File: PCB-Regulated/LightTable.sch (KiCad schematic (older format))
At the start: 22 parts, among them CON1 BARREL_JACK, P1 CONN_2_V, P2 CONN_01X01, P3 CONN_01X01, P4 CONN_01X01, P5 CONN_01X01, P6 CONN_01X01, P7 CONN_01X01, P8 CONN_4_V, U1 MosfetIRF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

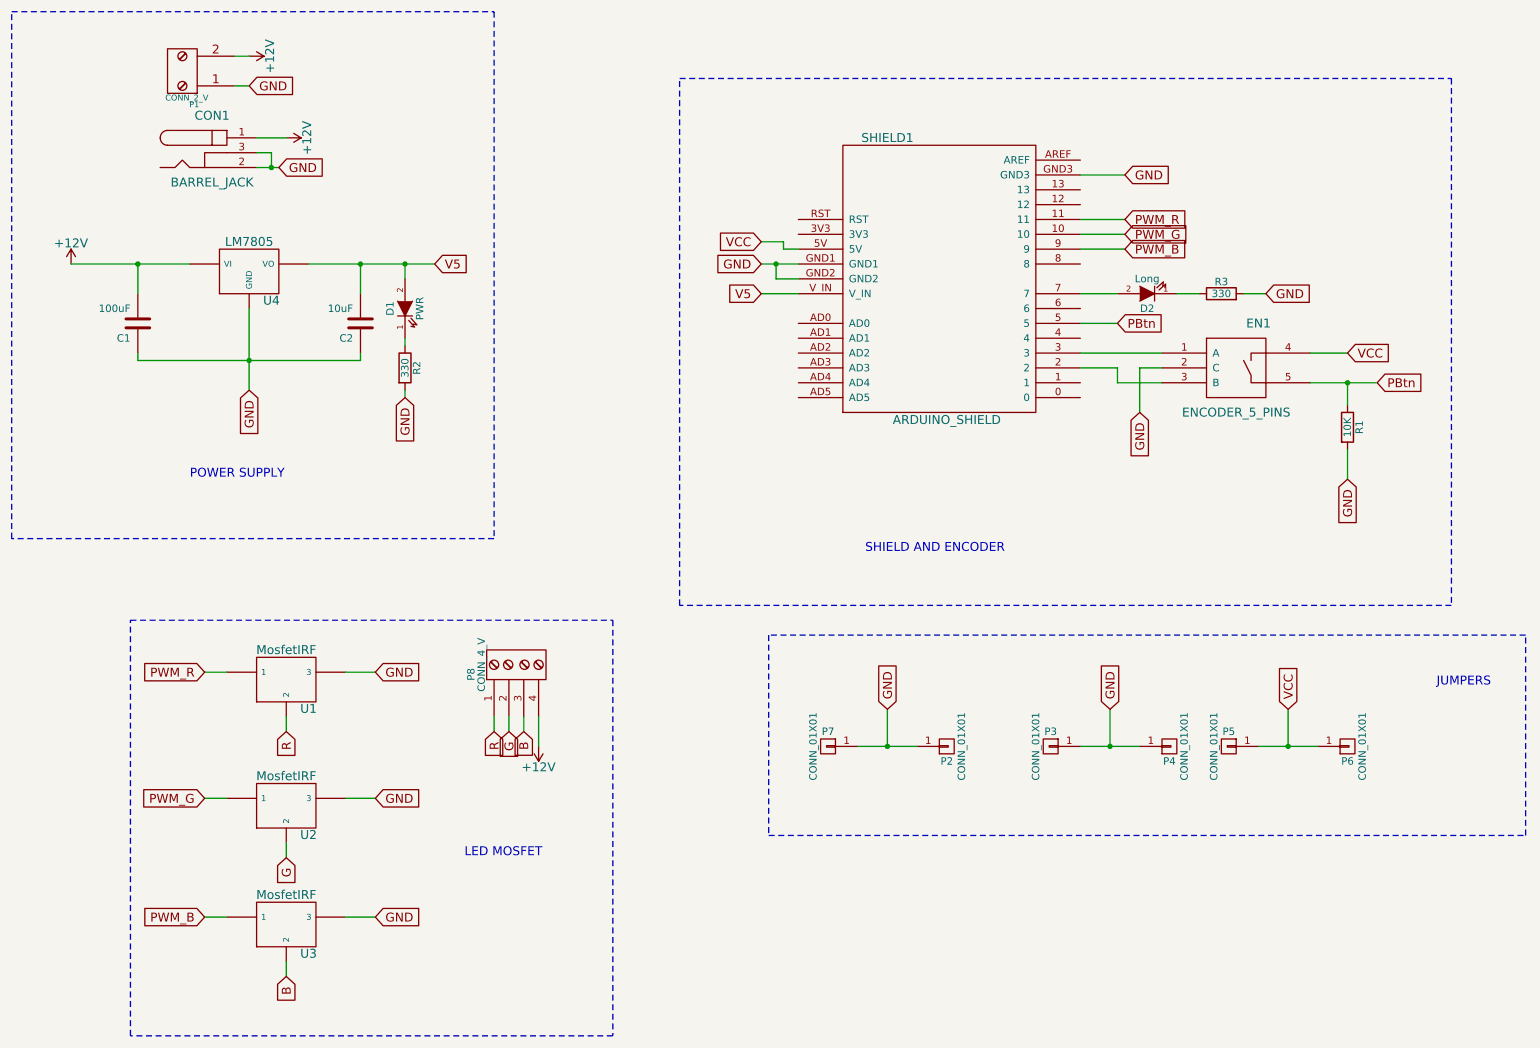
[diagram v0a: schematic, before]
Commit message: Fixed wrong placement of shield
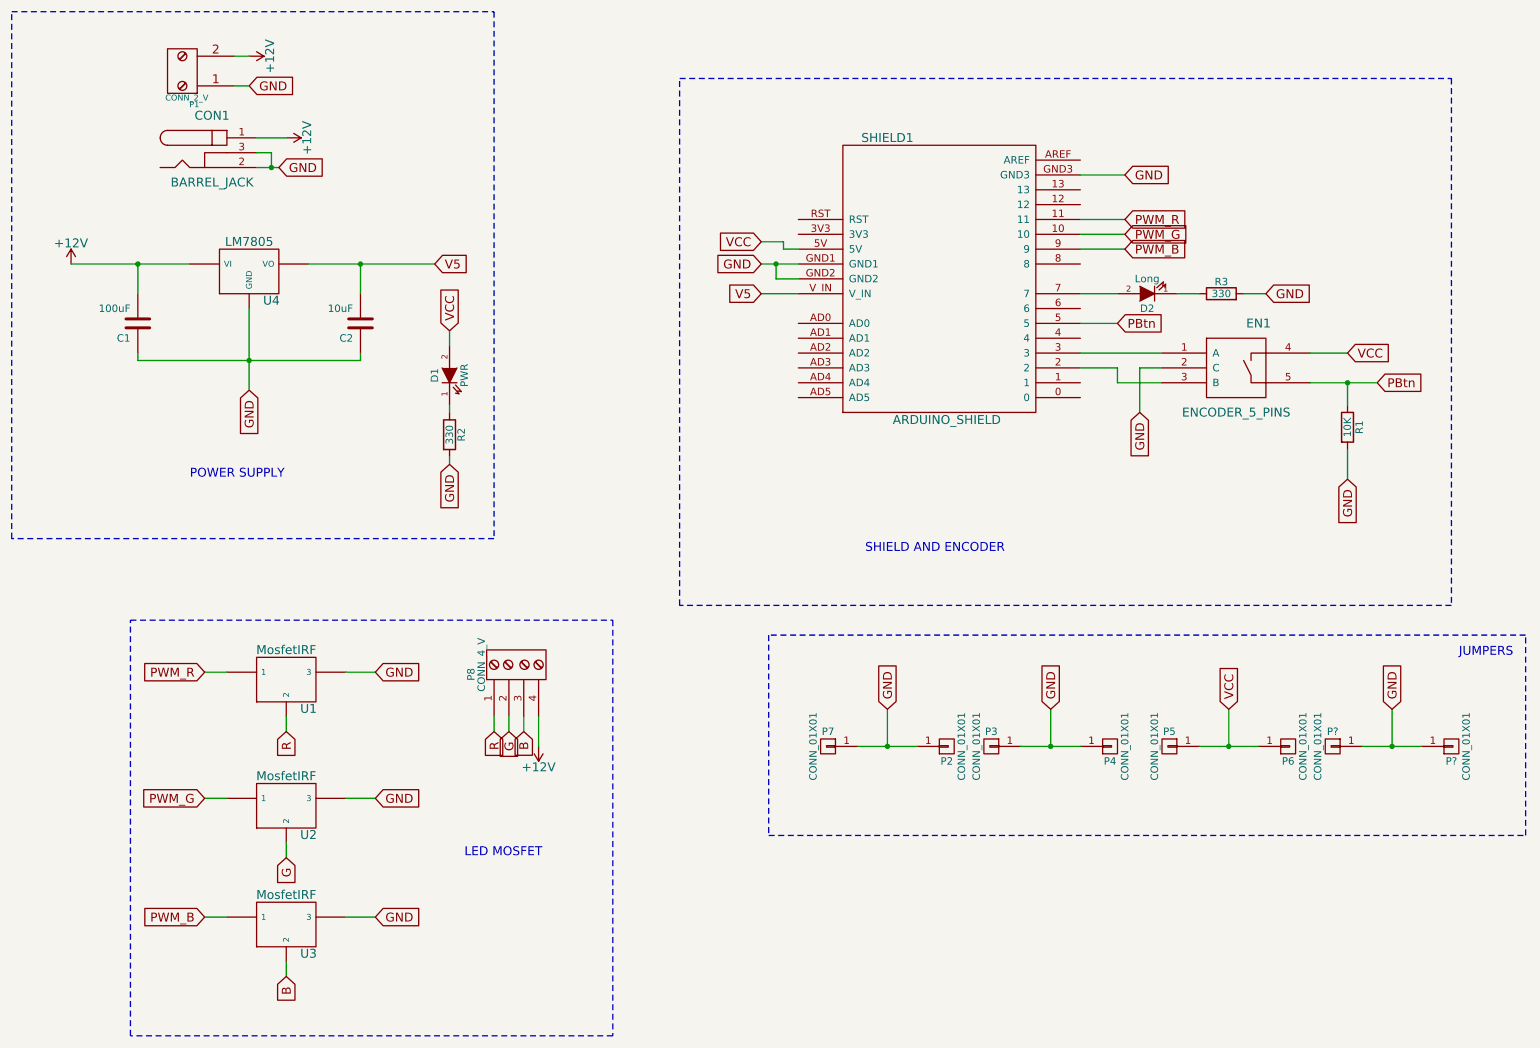
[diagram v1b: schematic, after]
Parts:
- added P? (x2): CONN_01X01, library:header1x01, symbol CONN_01X01
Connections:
- net GND: now also P?.1 (P1), P?.1 (P1)
- net V5: no longer D1.2 (A)
- net VCC: now also D1.2 (A)
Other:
- moved on the sheet: D1, P3, P4, P5, P6, R2
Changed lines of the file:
@@
 L CONN_01X01 P4
 U 1 1 55CC9A8E
-P 8350 5550
-F 0 "P4" H 8350 5650 50  0000 C CNN
-F 1 "CONN_01X01" V 8450 5550 50  0000 C CNN
-F 2 "library:header1x01" H 8350 5550 60  0001 C CNN
-F 3 "" H 8350 5550 60  0000 C CNN
-	1    8350 5550
+P 7950 5550
+F 0 "P4" H 7950 5650 50  0000 C CNN
+F 1 "CONN_01X01" V 8050 5550 50  0000 C CNN
+F 2 "library:header1x01" H 7950 5550 60  0001 C CNN
+F 3 "" H 7950 5550 60  0000 C CNN
+	1    7950 5550
 	1    0    0    1
 $EndComp
@@
 L CONN_01X01 P3
 U 1 1 55CC9A94
-P 7550 5550
-F 0 "P3" H 7550 5650 50  0000 C CNN
-F 1 "CONN_01X01" V 7650 5550 50  0000 C CNN
-F 2 "library:header1x01" H 7550 5550 60  0001 C CNN
-F 3 "" H 7550 5550 60  0000 C CNN
-	1    7550 5550
+P 7150 5550
+F 0 "P3" H 7150 5650 50  0000 C CNN
+F 1 "CONN_01X01" V 7250 5550 50  0000 C CNN
+F 2 "library:header1x01" H 7150 5550 60  0001 C CNN
+F 3 "" H 7150 5550 60  0000 C CNN
+	1    7150 5550
 	-1   0    0    -1
 $EndComp
 Wire Wire Line
-	7750 5550 8150 5550
+	7350 5550 7750 5550
 Wire Wire Line
-	7950 5550 7950 5300
-Connection ~ 7950 5550
-Text GLabel 7950 5300 1    60   Input ~ 0
+	7550 5550 7550 5300
+Connection ~ 7550 5550
+Text GLabel 7550 5300 1    60   Input ~ 0
 GND
 $Comp
 L CONN_01X01 P6
 U 1 1 55CC9B1E
-P 9550 5550
-F 0 "P6" H 9550 5650 50  0000 C CNN
-F 1 "CONN_01X01" V 9650 5550 50  0000 C CNN
-F 2 "library:header1x01" H 9550 5550 60  0001 C CNN
-F 3 "" H 9550 5550 60  0000 C CNN
-	1    9550 5550
+P 9150 5550
+F 0 "P6" H 9150 5650 50  0000 C CNN
+F 1 "CONN_01X01" V 9250 5550 50  0000 C CNN
+F 2 "library:header1x01" H 9150 5550 60  0001 C CNN
+F 3 "" H 9150 5550 60  0000 C CNN
+	1    9150 5550
 	1    0    0    1
 $EndComp
@@
 L CONN_01X01 P5
 U 1 1 55CC9B24
-P 8750 5550
-F 0 "P5" H 8750 5650 50  0000 C CNN
-F 1 "CONN_01X01" V 8850 5550 50  0000 C CNN
-F 2 "library:header1x01" H 8750 5550 60  0001 C CNN
-F 3 "" H 8750 5550 60  0000 C CNN
-	1    8750 5550
+P 8350 5550
+F 0 "P5" H 8350 5650 50  0000 C CNN
+F 1 "CONN_01X01" V 8450 5550 50  0000 C CNN
+F 2 "library:header1x01" H 8350 5550 60  0001 C CNN
+F 3 "" H 8350 5550 60  0000 C CNN
+	1    8350 5550
 	-1   0    0    -1
 $EndComp
 Wire Wire Line
-	8950 5550 9350 5550
+	8550 5550 8950 5550
 Wire Wire Line
-	9150 5550 9150 5300
-Connection ~ 9150 5550
-Text GLabel 9150 5300 1    60   Input ~ 0
+	8750 5550 8750 5300
+Connection ~ 8750 5550
+Text GLabel 8750 5300 1    60   Input ~ 0
 VCC
 Wire Notes Line
@@
 Wire Notes Line
 	10750 4800 5650 4800
-Text Notes 10150 5150 0    60   ~ 0
+Text Notes 10300 4950 0    60   ~ 0
 JUMPERS
 $Comp
@@
 L LED D1
 U 1 1 55CC841D
-P 3200 2600
-F 0 "D1" H 3200 2700 50  0000 C CNN
-F 1 "PWR" H 3200 2500 50  0000 C CNN
-F 2 "LEDs:LED-5MM" H 3200 2600 60  0001 C CNN
-F 3 "" H 3200 2600 60  0000 C CNN
-	1    3200 2600
+P 3500 3050
+F 0 "D1" H 3500 3150 50  0000 C CNN
+F 1 "PWR" H 3500 2950 50  0000 C CNN
+F 2 "LEDs:LED-5MM" H 3500 3050 60  0001 C CNN
+F 3 "" H 3500 3050 60  0000 C CNN
+	1    3500 3050
 	0    -1   -1   0
 $EndComp
-Connection ~ 3200 2300
 $Comp
 L R R2
 U 1 1 55CC852C
-P 3200 3000
-F 0 "R2" V 3280 3000 50  0000 C CNN
-F 1 "330" V 3200 3000 50  0000 C CNN
-F 2 "Resistors_ThroughHole:Resistor_Horizontal_RM10mm" V 3130 3000 30  0001 C CNN
-F 3 "" H 3200 3000 30  0000 C CNN
-	1    3200 3000
+P 3500 3450
+F 0 "R2" V 3580 3450 50  0000 C CNN
+F 1 "330" V 3500 3450 50  0000 C CNN
+F 2 "Resistors_ThroughHole:Resistor_Horizontal_RM10mm" V 3430 3450 30  0001 C CNN
+F 3 "" H 3500 3450 30  0000 C CNN
+	1    3500 3450
 	1    0    0    -1
 $EndComp
-Text GLabel 3200 3200 3    60   Input ~ 0
+Text GLabel 3500 3650 3    60   Input ~ 0
 GND
 Wire Wire Line
-	3200 3200 3200 3150
+	3500 3650 3500 3600
 Wire Wire Line
-	3200 2850 3200 2800
-Wire Wire Line
-	3200 2400 3200 2300
+	3500 3300 3500 3250
 Text GLabel 8000 2700 2    60   Input ~ 0
 PBtn
@@
 Wire Wire Line
 	8850 2500 9000 2500
+Text GLabel 3500 2750 1    60   Input ~ 0
+VCC
+Wire Wire Line
+	3500 2750 3500 2850
+$Comp
+L CONN_01X01 P?
+U 1 1 55D5B06A
+P 10250 5550
+F 0 "P?" H 10250 5650 50  0000 C CNN
+F 1 "CONN_01X01" V 10350 5550 50  0000 C CNN
+F 2 "library:header1x01" H 10250 5550 60  0001 C CNN
+F 3 "" H 10250 5550 60  0000 C CNN
+	1    10250 5550
+	1    0    0    1
+$EndComp
+$Comp
+L CONN_01X01 P?
+U 1 1 55D5B070
+P 9450 5550
+F 0 "P?" H 9450 5650 50  0000 C CNN
+F 1 "CONN_01X01" V 9550 5550 50  0000 C CNN
+F 2 "library:header1x01" H 9450 5550 60  0001 C CNN
+F 3 "" H 9450 5550 60  0000 C CNN
+	1    9450 5550
+	-1   0    0    -1
+$EndComp
+Wire Wire Line
+	9650 5550 10050 5550
+Wire Wire Line
+	9850 5550 9850 5300
+Connection ~ 9850 5550
+Text GLabel 9850 5300 1    60   Input ~ 0
+GND
 $EndSCHEMATC

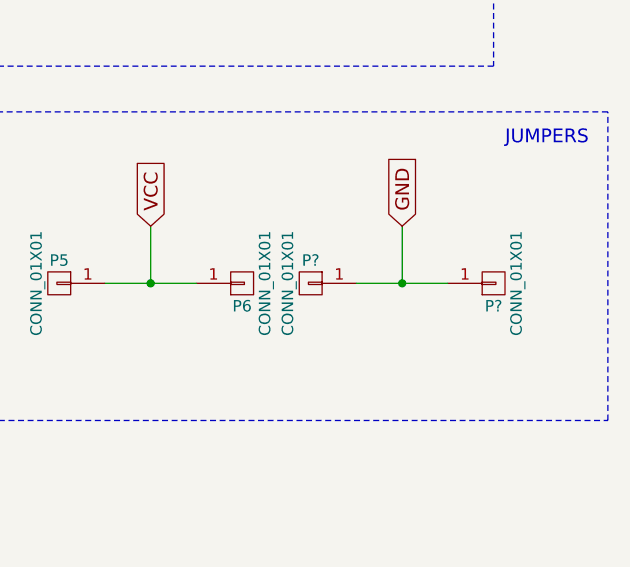
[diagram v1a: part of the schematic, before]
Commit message: Added GND jumper to improve ground connectivity
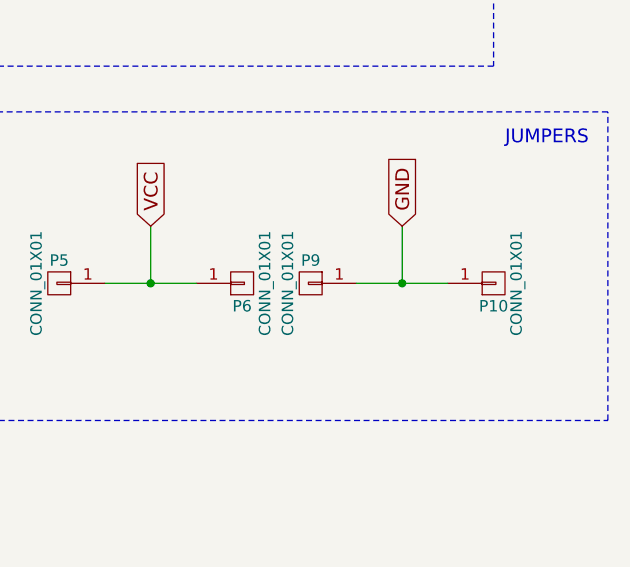
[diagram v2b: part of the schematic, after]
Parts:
- gave numbers to parts that had none: 2
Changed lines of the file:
@@
 	3500 2750 3500 2850
 $Comp
-L CONN_01X01 P?
+L CONN_01X01 P10
 U 1 1 55D5B06A
 P 10250 5550
-F 0 "P?" H 10250 5650 50  0000 C CNN
+F 0 "P10" H 10250 5650 50  0000 C CNN
 F 1 "CONN_01X01" V 10350 5550 50  0000 C CNN
 F 2 "library:header1x01" H 10250 5550 60  0001 C CNN
@@
 $EndComp
 $Comp
-L CONN_01X01 P?
+L CONN_01X01 P9
 U 1 1 55D5B070
 P 9450 5550
-F 0 "P?" H 9450 5650 50  0000 C CNN
+F 0 "P9" H 9450 5650 50  0000 C CNN
 F 1 "CONN_01X01" V 9550 5550 50  0000 C CNN
 F 2 "library:header1x01" H 9450 5550 60  0001 C CNN
